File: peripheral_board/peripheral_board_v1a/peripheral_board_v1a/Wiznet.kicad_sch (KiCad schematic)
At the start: 38 parts, among them SW3 3_Pin_Dip_Switch_DSWB03LHGET_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, U4 W5500, U5 SN74AHC1G125DBVR, Y2 25MHz

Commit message: PCB Update
Got all the parts on the board placed. Now just finishing the routing for each interconnection.
Trying to maintain a side to side/up to down but the board kinda follows it. For each plane  there is fill zones that will be for the chip that is on the top. Some of the traces are just being fed to where they need to go but the important EMI signals are being contained to their guidelines.
I will need to look at the lengths of the traces to make sure they are kept around the same length.

Will need to go over the board with some other eyes to make sure its ok.

I made sure the Wiznet traces are the same as SALAD.
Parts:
- renumbered C68 to C22, C67 to C23, C23 to C24, C24 to C25, C22 to C26, C26 to C27, C27 to C28, C25 to C29, C28 to C30, C29 to C31, C30 to C32, C31 to C33, C32 to C34, C33 to C35

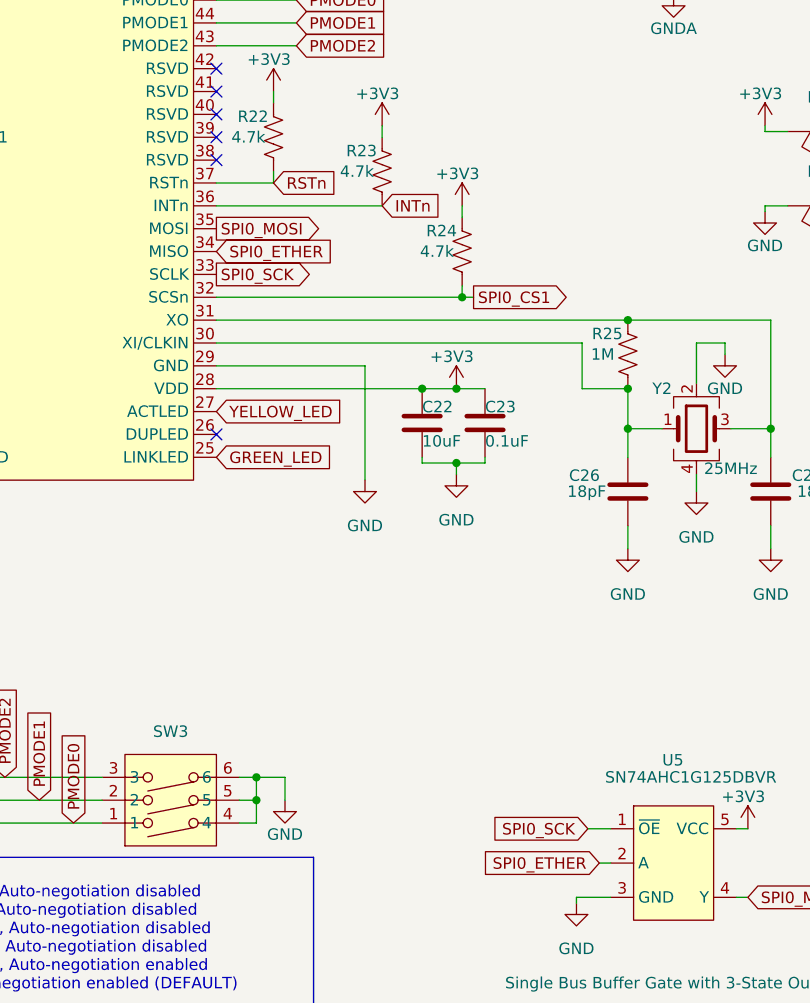
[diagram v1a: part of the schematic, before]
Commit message: PCB almost done
Finished the routing except for the power board connector. Will be looking into adding in a Power path controller or similar. Want to add in via stitching for the DP signals. Should be just about done it would be more of just doing some change/improvements.
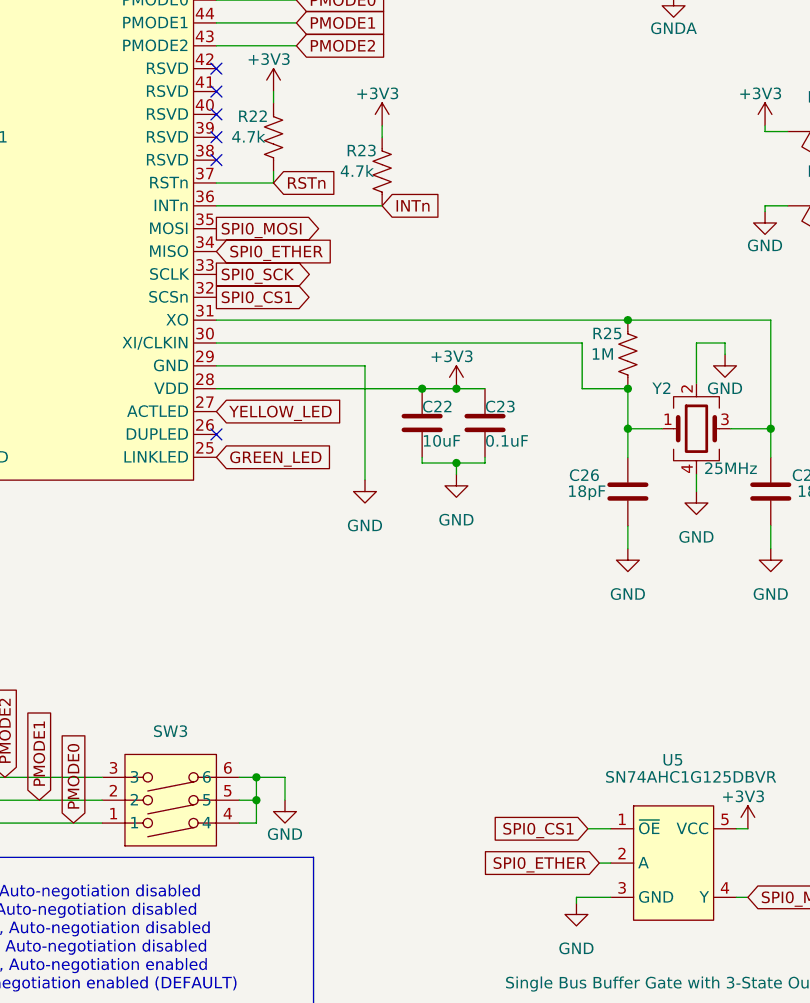
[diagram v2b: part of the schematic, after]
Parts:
- removed R24: 4.7k, Resistor_SMD:R_0603_1608Metric, symbol Device:R_US
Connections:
- net SPI0_CS1: now also U5.1 (~{OE})
- net SPI0_SCK: no longer U5.1 (~{OE})

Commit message: Part picking for board
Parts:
- C21, C23, C24, C25, C27, C28: value 0.1uF -> 100nF
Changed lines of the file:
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@@
 			)
 		)
-		(property "Value" "0.1uF"
+		(property "Value" "100nF"
 			(at 24.511 85.725 90)
 			(effects
@@
 			)
 		)
-		(property "Value" "0.1uF"
+		(property "Value" "100nF"
 			(at 132.715 33.782 0)
 			(effects
@@
 			)
 		)
-		(property "Value" "0.1uF"
+		(property "Value" "100nF"
 			(at 120.015 33.782 0)
 			(effects
@@
 			)
 		)
-		(property "Value" "0.1uF"
+		(property "Value" "100nF"
 			(at 126.365 33.782 0)
 			(effects
@@
 			)
 		)
-		(property "Value" "0.1uF"
+		(property "Value" "100nF"
 			(at 105.41 87.757 0)
 			(effects
@@
 			)
 		)
-		(property "Value" "0.1uF"
+		(property "Value" "100nF"
 			(at 113.03 33.782 0)
 			(effects
